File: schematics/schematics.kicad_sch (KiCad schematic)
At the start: 11 parts, among them U1 74LVC1G86, U2 ESP32-C3_SUPERMINI_TH

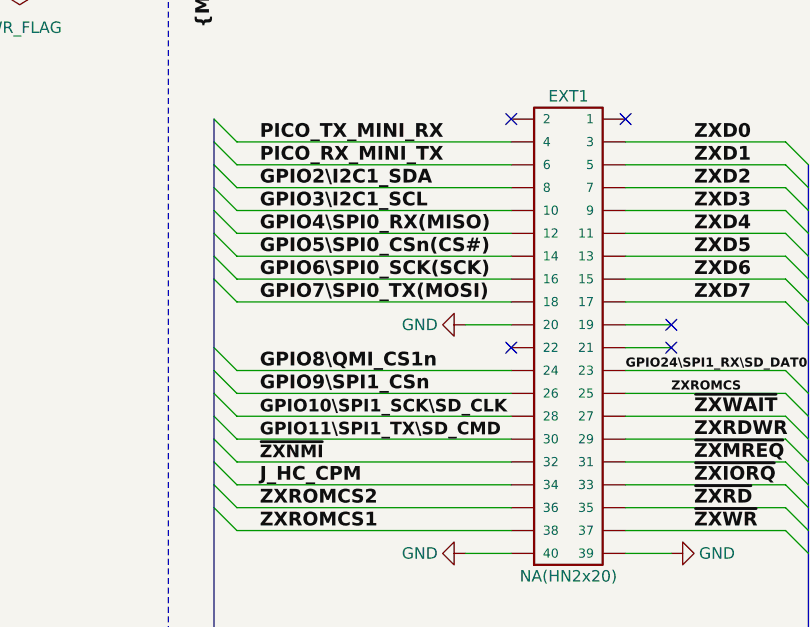
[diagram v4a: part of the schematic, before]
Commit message: Fix BogDan is an idiot wrong line assignment
Fixes: #1, #3
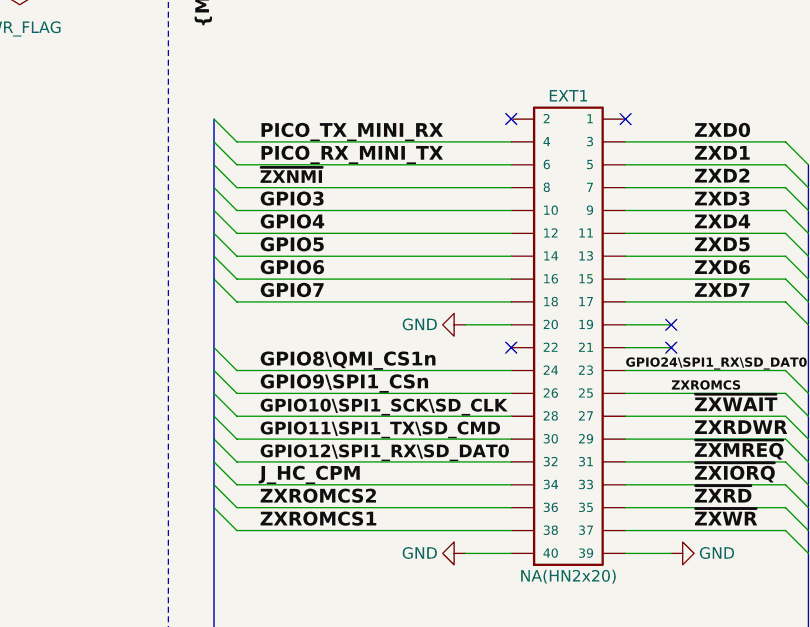
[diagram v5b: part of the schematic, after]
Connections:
- net GPIO2\I2C1_SDA is gone; now on net ~{ZXNMI}: EXT1.8
- net ~{ZXNMI}: no longer EXT1.32
- net GPIO3\I2C1_SCL renamed GPIO3
- net GPIO4\SPI0_RX(MISO) renamed GPIO4
- net GPIO5\SPI0_CSn(CS#) renamed GPIO5
- net GPIO6\SPI0_SCK(SCK) renamed GPIO6
- net GPIO7\SPI0_TX(MOSI) renamed GPIO7
- new net GPIO12\SPI1_RX\SD_DAT0: EXT1.32
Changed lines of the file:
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@@
-		)
-	)
-	(label "~{ZXNMI}"
-		(at 114.3 80.01 0)
-		(effects
-			(font
-				(size 1.397 1.397)
-				(thickness 0.3048)
-				(bold yes)
-			)
-			(justify left bottom)
 		)
 	)
@@
 		)
 	)
-	(label "GPIO5\\SPI0_CSn(CS#)"
+	(label "GPIO5"
 		(at 114.3 57.15 0)
 		(effects
@@
 		)
 	)
-	(label "GPIO2\\I2C1_SDA"
-		(at 114.3 49.53 0)
-		(effects
-			(font
-				(size 1.524 1.524)
-				(thickness 0.3048)
-				(bold yes)
-			)
-			(justify left bottom)
-		)
-	)
 	(label "QSPI_CLK"
 		(at 220.98 80.01 0)
@@
 		)
 	)
-	(label "GPIO7\\SPI0_TX(MOSI)"
+	(label "GPIO7"
 		(at 114.3 62.23 0)
 		(effects
@@
 		)
 	)
+	(label "GPIO12\\SPI1_RX\\SD_DAT0"
+		(at 114.3 80.01 0)
+		(effects
+			(font
+				(size 1.397 1.397)
+				(thickness 0.3048)
+				(bold yes)
+			)
+			(justify left bottom)
+		)
+	)
 	(label "ZXA2"
 		(at 266.7 49.53 180)
@@
 		)
 	)
-	(label "GPIO4\\SPI0_RX(MISO)"
+	(label "GPIO4"
 		(at 114.3 54.61 0)
 		(effects
@@
 		)
 	)
-	(label "GPIO3\\I2C1_SCL"
+	(label "GPIO3"
 		(at 114.3 52.07 0)
 		(effects
@@
 		)
 	)
-	(label "GPIO6\\SPI0_SCK(SCK)"
+	(label "GPIO6"
 		(at 114.3 59.69 0)
 		(effects
@@
 				(thickness 0.3048)
 				(bold yes)
+			)
+			(justify left bottom)
+		)
+	)
+	(label "~{ZXNMI}"
+		(at 114.3 49.53 0)
+		(effects
+			(font
+				(size 1.397 1.397)
+				(thickness 0.3048)
+				(bold yes)

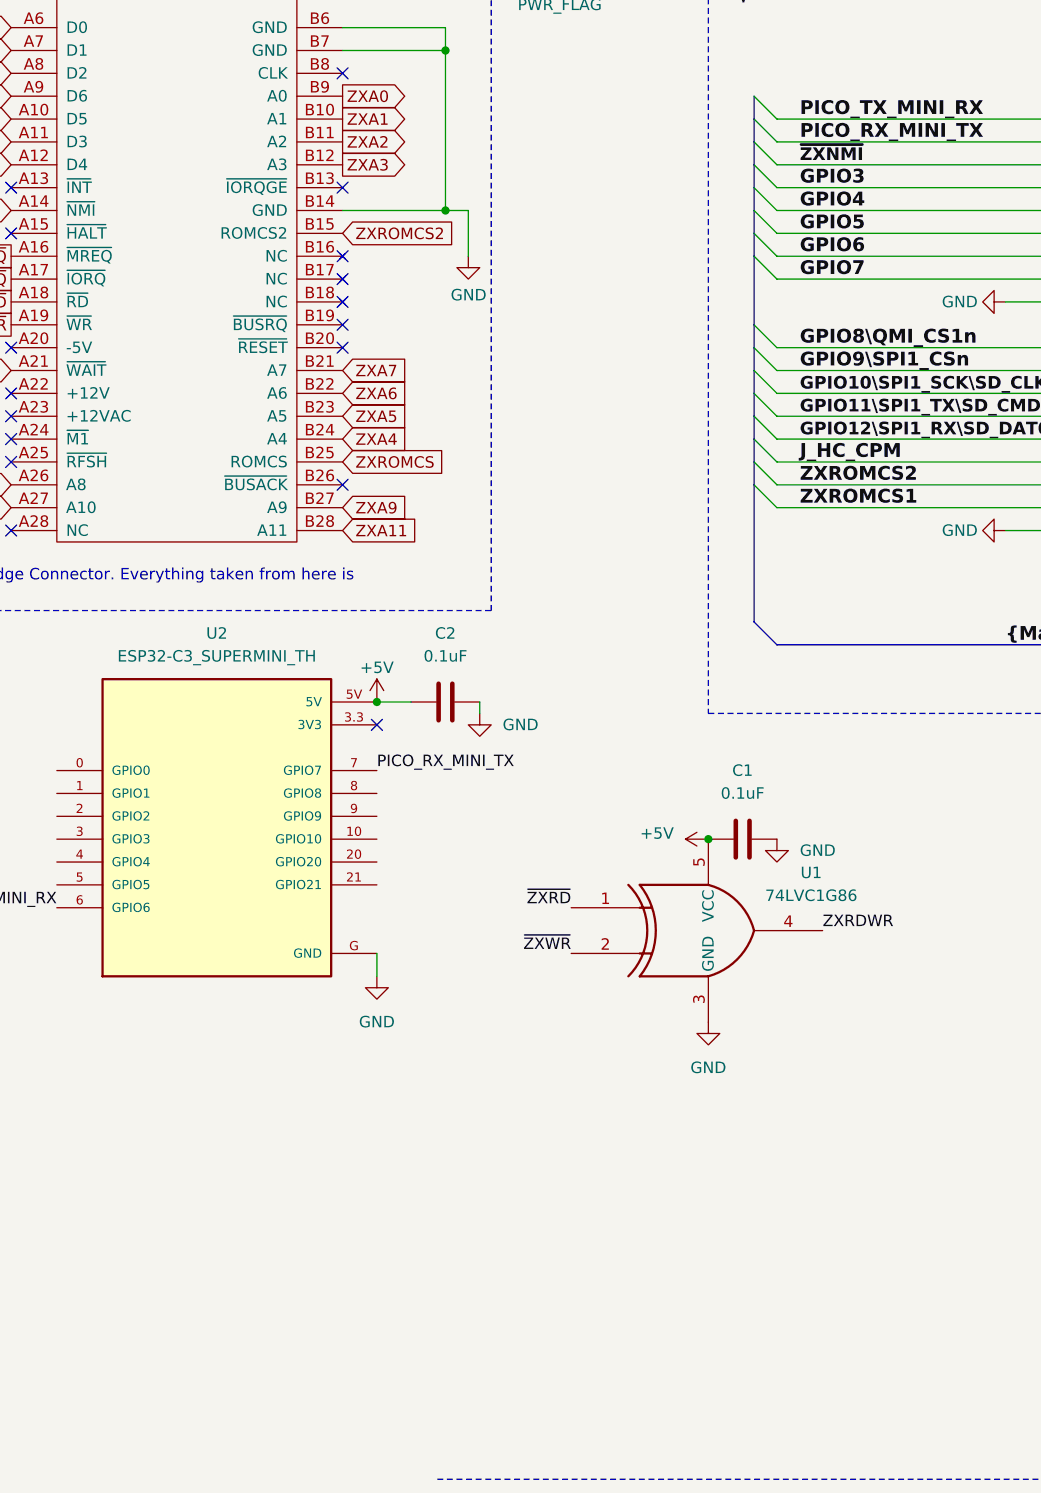
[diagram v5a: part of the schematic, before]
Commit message: Add kempston joystick
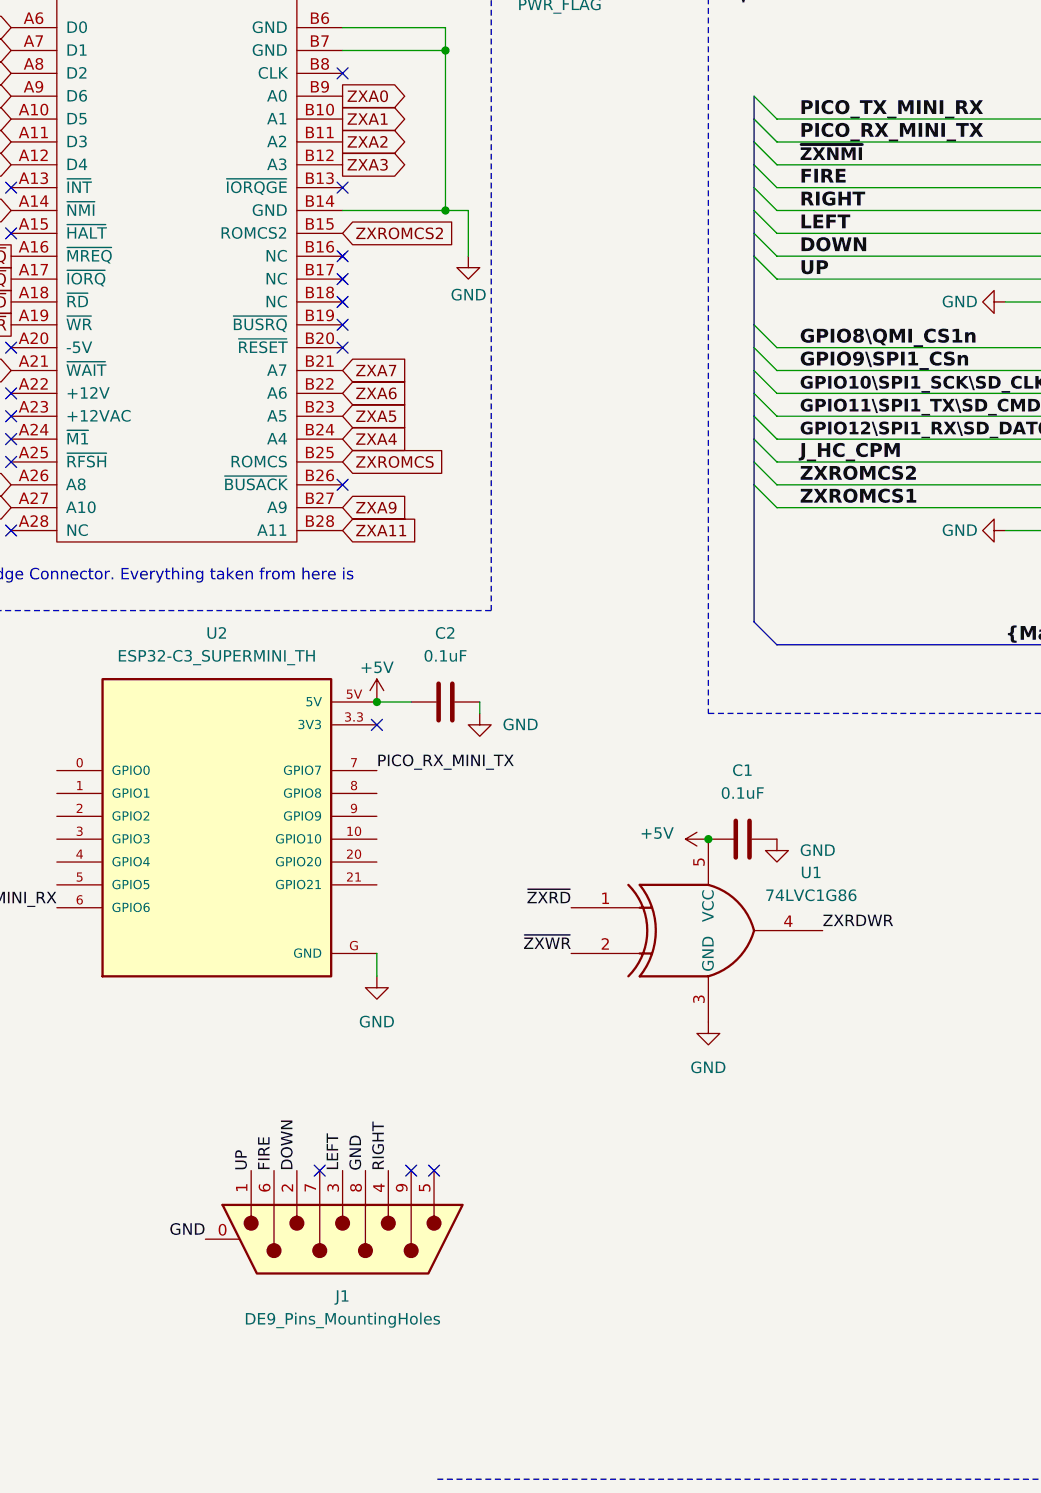
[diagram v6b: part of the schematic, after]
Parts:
- added J1: DE9_Pins_MountingHoles, Connector_Dsub:DSUB-9_Pins_Horizontal_P2.77x2.84mm_EdgePinOffset4.94mm_Housed_MountingHolesOffset4.94mm, symbol Connector:DE9_Pins_MountingHoles
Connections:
- net GND: now also J1.0 (PAD), J1.8
- net GPIO3 renamed FIRE
- net FIRE: now also J1.6
- net GPIO4 renamed RIGHT
- net RIGHT: now also J1.4
- net GPIO5 renamed LEFT
- net LEFT: now also J1.3
- net GPIO6 renamed DOWN
- net DOWN: now also J1.2
- net GPIO7 renamed UP
- net UP: now also J1.1
- no-connect marks 30 -> 33
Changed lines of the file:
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@@
 	)
 	(no_connect
+		(at 60.96 161.29)
+	)
+	(no_connect
 		(at 160.02 67.31)
 	)
@@
 	)
 	(no_connect
+		(at 71.12 161.29)
+	)
+	(no_connect
 		(at 26.67 77.47)
 	)
@@
 		(at 160.02 64.77)
 	)
+	(no_connect
+		(at 73.66 161.29)
+	)
 	(bus_entry
 		(at 271.78 59.69)
@@
 		)
 	)
-	(label "GPIO5"
+	(label "LEFT"
 		(at 114.3 57.15 0)
 		(effects
@@
 		)
 	)
-	(label "GPIO7"
+	(label "UP"
 		(at 114.3 62.23 0)
 		(effects
@@
 		)
 	)
+	(label "FIRE"
+		(at 55.88 161.29 90)
+		(effects
+			(font
+				(size 1.27 1.27)
+			)
+			(justify left bottom)
+		)
+	)
 	(label "ZXD6"
 		(at 162.56 59.69 0)
@@
 		)
 	)
-	(label "GPIO4"
+	(label "RIGHT"
 		(at 114.3 54.61 0)
 		(effects
@@
 		)
 	)
-	(label "GPIO3"
+	(label "FIRE"
 		(at 114.3 52.07 0)
 		(effects
@@
 		)
 	)
+	(label "LEFT"
+		(at 63.5 161.29 90)
+		(effects
+			(font
+				(size 1.27 1.27)
+			)
+			(justify left bottom)
+		)
+	)
 	(label "ZXRDWR"
 		(at 116.84 134.62 0)
@@
 		)
 	)
+	(label "GND"
+		(at 66.04 161.29 90)
+		(effects
+			(font
+				(size 1.27 1.27)
+			)
+			(justify left bottom)
+		)
+	)
 	(label "ZXA8"
 		(at 266.7 69.85 180)
@@
 		)
 	)
+	(label "UP"
+		(at 53.34 161.29 90)
+		(effects
+			(font
+				(size 1.27 1.27)
+			)
+			(justify left bottom)
+		)
+	)
 	(label "RUN"
 		(at 220.98 62.23 0)
@@
 		)
 	)
-	(label "GPIO6"
+	(label "DOWN"
+		(at 58.42 161.29 90)
+		(effects
+			(font
+				(size 1.27 1.27)
+			)
+			(justify left bottom)
+		)
+	)
+	(label "DOWN"
 		(at 114.3 59.69 0)
 		(effects
@@
 		)
 	)
+	(label "RIGHT"
+		(at 68.58 161.29 90)
+		(effects
+			(font
+				(size 1.27 1.27)
+			)
+			(justify left bottom)
+		)
+	)
 	(label "J_HC_CPM"
 		(at 187.96 125.73 0)
@@
 		)
 	)
+	(label "GND"
+		(at 48.26 168.91 180)
+		(effects
+			(font
+				(size 1.27 1.27)
+			)
+			(justify right bottom)
+		)
+	)
 	(label "~{ZXRD}"
 		(at 162.56 85.09 0)
@@
 					(unit 1)
 				)
+			)
+		)
+	)
+	(symbol
+		(lib_id "Connector:DE9_Pins_MountingHoles")
+		(at 63.5 168.91 270)
+		(unit 1)
+		(exclude_from_sim no)
+		(in_bom yes)
+		(on_board yes)
+		(dnp no)
+		(fields_autoplaced yes)
+		(property "Reference" "J1"
+			(at 63.5 175.26 90)
+			(effects
+				(font
+					(size 1.27 1.27)
+				)
+			)
+		)
+		(property "Value" "DE9_Pins_MountingHoles"
+			(at 63.5 177.8 90)
+			(effects
+				(font
+					(size 1.27 1.27)
+				)
+			)
+		)
+		(property "Footprint" "Connector_Dsub:DSUB-9_Pins_Horizontal_P2.77x2.84mm_EdgePinOffset4.94mm_Housed_MountingHolesOffset4.94mm"
+			(at 63.5 168.91 0)
+			(effects
+				(font
+					(size 1.27 1.27)
+				)
+				(hide yes)
+			)
+		)
+		(property "Datasheet" "~"
+			(at 63.5 168.91 0)
+			(effects
+				(font
+					(size 1.27 1.27)
+				)
+				(hide yes)
+			)
+		)
+		(property "Description" "9-pin D-SUB connector, pins (male), Mounting Hole"
+			(at 63.5 168.91 0)
+			(effects
+				(font
+					(size 1.27 1.27)
+				)
+				(hide yes)
+			)
+		)
+		(pin "0"
+		)
+		(pin "4"
+		)
+		(pin "1"
+		)
+		(pin "3"
+		)
+		(pin "8"
+		)
+		(pin "6"
+		)
+		(pin "5"
+		)
+		(pin "7"
+		)
+		(pin "2"
+		)
+		(pin "9"
+		)
+		(instances
+			(project ""
+				(path "/9a328648-77a9-433b-92be-70cc38e5a83b"
+					(reference "J1")
+					(unit 1)
+				)
